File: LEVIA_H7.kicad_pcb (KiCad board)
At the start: 6 copper layers, 36.7 x 36.7 mm, 134 parts, among them J1 TF-028-H265, Q1 AO3400A, SW1 SW_Push, U1 USBLC6-2P6, U10 ZX-SH1.0-4PWT, U11 ZX-SH1.0-3PWT, U12 SIT1051TK/3, U13 ZX-SH1.0-4PWT, U14 ICM-42688-P, U15 ICM-42688-P, U16 DPS368XTSA1, U17 IST8310, U18 ZX-SH1.0-4PWT, U19 ZX-SH1.0-6PWT, U2 STM32H743VIHx, U20 ZX-SH1.0-6PWT, U21 ZX-SH1.0-3PWT, U22 ZX-SH1.0-8PWT, U24 ZX-SH1.0-4PWT, U3 ZX-SH1.0-4PWT, U4 LMR43620R5RPER, U5 LMR604303SRAKRQ1, U6 AP7361C-33FGE-7, U7 AP7361C-33FGE-7, U8 ZX-SH1.0-4PWT, U9 AT7456ELAH, Y1 8MHz, Y2 XL7EL89COI-111YLC-27M

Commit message: BME280
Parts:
- removed R33: 10K, Resistor_SMD:R_0402_1005Metric
- added C55: 100n, Capacitor_SMD:C_0402_1005Metric, B.Cu at (147.2, 74.1)
- added C56: 100n, Capacitor_SMD:C_0402_1005Metric, B.Cu at (147.2, 75.9)
- added JP2: SolderJumper_2_Open, _pico:SolderJumper_Mini, B.Cu at (149.2, 75.4)
- added TP10: ~, EasyEDA:TestPoint_Pad_1.8x0.9mm, B.Cu at (149.2, 52.0)
- added TP3: ~, EasyEDA:TestPoint_Pad_1.8x0.9mm, B.Cu at (147.8, 52.0)
- added TP4: ~, EasyEDA:TestPoint_Pad_1.8x0.9mm, B.Cu at (146.5, 52.0)
- added TP5: ~, EasyEDA:TestPoint_Pad_1.8x0.9mm, B.Cu at (145.1, 52.0)
- added TP6: ~, EasyEDA:TestPoint_Pad_1.8x0.9mm, B.Cu at (143.8, 52.0)
- added TP7: ~, EasyEDA:TestPoint_Pad_1.8x0.9mm, B.Cu at (142.4, 52.0)
- added TP8: ~, EasyEDA:TestPoint_Pad_1.8x0.9mm, B.Cu at (141.1, 52.0)
- added TP9: ~, EasyEDA:TestPoint_Pad_1.8x0.9mm, B.Cu at (150.5, 52.0)
- added U25: BME680, Package_LGA:Bosch_LGA-8_3x3mm_P0.8mm_ClockwisePinNumbering, B.Cu at (145.0, 74.9)
- C1, C17, R10, R11, U11: moved to F.Cu
- R1, R2: moved to B.Cu
- moved U10 30.8 mm to (154.2, 65.7), turned to 90 degrees
- moved USB1 28.3 mm to (124.9, 60.7), turned to -90 degrees
- moved R1 26.4 mm to (124.0, 58.5), turned to 90 degrees
- moved U1 25.8 mm to (125.8, 60.5), turned to 0 degrees
- moved R2 25.3 mm to (123.8, 63.5), turned to 90 degrees
- moved U11 21.2 mm to (154.1, 72.7), turned to 90 degrees
- moved R11 9.94 mm to (148.3, 59.8)
- moved R22 9.83 mm to (149.8, 64.4), turned to 180 degrees
- moved R23 9.51 mm to (150.3, 69.6), turned to -90 degrees
- moved R10 9.32 mm to (148.7, 58.4), turned to 180 degrees
- moved C36 9.24 mm to (149.8, 65.3), turned to 0 degrees
- moved C37 8.79 mm to (149.8, 66.2), turned to 0 degrees
- moved C17 8.69 mm to (149.2, 59.8)
- moved C35 8.51 mm to (149.8, 67.2), turned to 0 degrees
- moved C38 8.50 mm to (149.8, 68.2), turned to 0 degrees
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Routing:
- net /MCU/USB_OTG_P.DN: track 0.00 -> 16.9 mm, vias 0 -> 1
- net /MCU/USB_OTG_P.DP: track 0.00 -> 16.1 mm, vias 0 -> 1
- net /I2C1|SPI3/SPI3.CS1: track 0.00 -> 14.5 mm, vias 0 -> 2
- net /MCU/SPI1.MOSI: track 0.00 -> 13.8 mm, vias 0 -> 2
- net /MCU/SDIO.D3: track 0.00 -> 13.7 mm
- net /MCU/SDIO.CMD: track 0.00 -> 13.6 mm, vias 0 -> 2
- net /I2C1|SPI3/SPI3.MOSI: track 0.00 -> 12.8 mm, vias 0 -> 1
- net /MCU/I2C2.SDA: track 0.00 -> 12.3 mm, vias 0 -> 1
- net /MCU/I2C2.SCL: track 0.00 -> 12.3 mm, vias 0 -> 2
- net /ANALOG VTX/SPI2.SCLK: track 0.00 -> 12.1 mm
- net +3V3_MCU: track 0.00 -> 11.8 mm, vias 0 -> 4
- net /MCU/VDD: track 1.10 -> 12.8 mm, vias 1 -> 3
- net /MCU/SDIO.D1: track 0.00 -> 11.0 mm
- net /MCU/SPI4.MOSI: track 0.00 -> 10.8 mm, vias 0 -> 2
- net /ANALOG VTX/SPI2.CS: track 0.00 -> 10.7 mm, vias 0 -> 2
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
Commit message: save
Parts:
- moved C6 0.23 mm to (132.6, 79.6)
- moved NT4 0.08 mm to (134.2, 77.4)
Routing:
- net /MCU/SPI4.CS: track 0.00 -> 10.7 mm, vias 0 -> 2
- net GND: track 0.00 -> 5.63 mm, vias 0 -> 4
- net /MCU/SWDIO: track 4.32 -> 6.12 mm
- net /MCU/SPI1.CS: track 9.79 -> 10.9 mm
- net /MCU/VDD: track 12.8 -> 13.6 mm

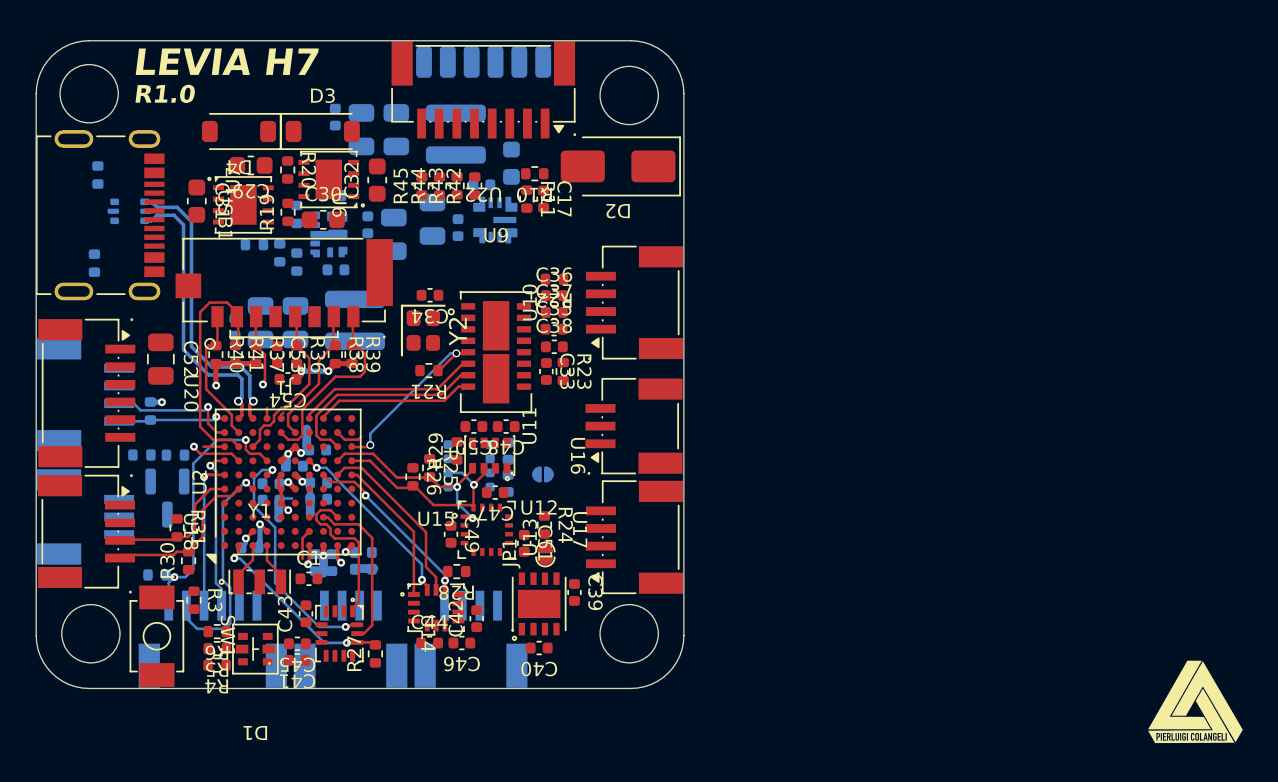
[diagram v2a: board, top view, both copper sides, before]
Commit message: fixed edge and hole positions
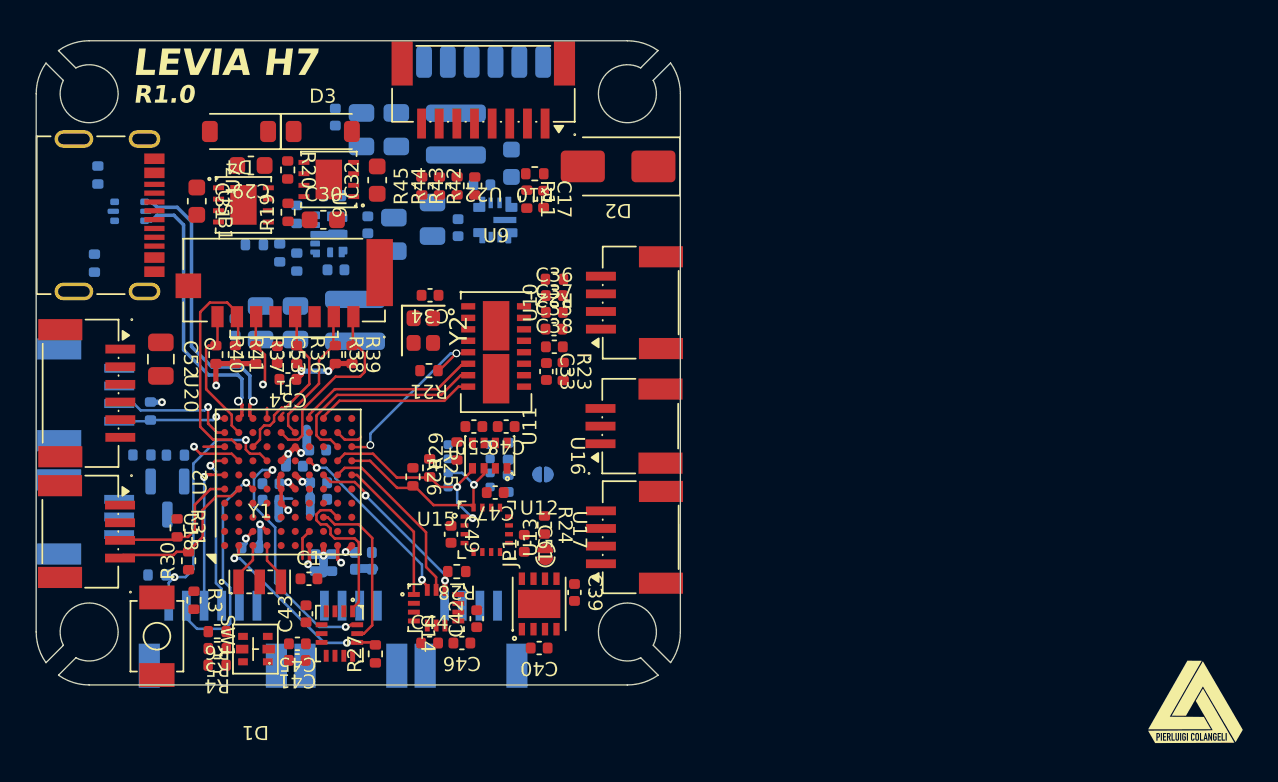
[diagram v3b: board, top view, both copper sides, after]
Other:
- board size 36.7 x 36.7 mm -> 36.5 x 36.5 mm

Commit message: routing
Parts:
- moved R30 8.42 mm to (126.9, 72.2)
- moved U18 8.34 mm to (123.6, 70.3)
- moved R31 8.32 mm to (126.9, 70.3)
- moved C9 7.31 mm to (140.8, 74.1)
- moved U20 7.17 mm to (123.6, 78.0)
- moved C52 5.94 mm to (127.3, 74.8), turned to 90 degrees
- moved R35 5.87 mm to (127.3, 80.1)
- moved R34 4.96 mm to (127.3, 79.2), turned to 0 degrees
- moved C39 2.64 mm to (150.6, 79.5), turned to 90 degrees
- moved NT4 2.35 mm to (136.5, 77.7), turned to 0 degrees
- moved C8 1.79 mm to (137.0, 72.4)
- moved NT5 1.20 mm to (135.1, 72.4), turned to 0 degrees
- moved C40 0.93 mm to (149.9, 85.2), turned to -90 degrees
- moved C43 0.85 mm to (135.2, 84.0), turned to 180 degrees
- moved U12 0.70 mm to (149.6, 82.4)
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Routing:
- net /MCU/ADC1_CURR1: track 0.00 -> 61.2 mm, vias 0 -> 2
- net /MCU/ADC1_VBAT1: track 0.00 -> 50.3 mm, vias 0 -> 1
- net /CAN/CAN1.SILENT: track 0.00 -> 48.5 mm, vias 0 -> 2
- net /MCU/UART8.RX: track 0.00 -> 43.4 mm, vias 0 -> 1
- net /CAN/CAN1.TX: track 0.00 -> 34.4 mm, vias 0 -> 2
- net /CAN/CAN1.RX: track 0.00 -> 30.0 mm, vias 0 -> 2
- net /MCU/9V_EN: track 0.00 -> 26.3 mm, vias 0 -> 1
- net /ANALOG VTX/UART1.TX: track 0.00 -> 23.4 mm, vias 0 -> 2
- net /MCU/UART6.RX: track 0.37 -> 22.6 mm, vias 0 -> 2
- net /MCU/UART6.TX: track 0.00 -> 22.0 mm, vias 0 -> 2
- net /MCU/GYRO2_CLKIN: track 0.00 -> 17.2 mm, vias 0 -> 2
- net /MCU/GYRO1_CLKIN: track 0.00 -> 15.5 mm, vias 0 -> 2
- net /MCU/GYRO2_EXTI: track 0.00 -> 13.9 mm, vias 0 -> 2
- net /MCU/UART2.TX: track 0.00 -> 13.5 mm, vias 0 -> 2
- net /MCU/UART2.RX: track 0.00 -> 11.6 mm, vias 0 -> 2
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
